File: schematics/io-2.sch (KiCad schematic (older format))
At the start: 8 parts, among them J13 FDC Connector, J13 Left Audio, J14 Right Audio, J9 IDE Connector, U11 WD1772, U12 EN5503DOC

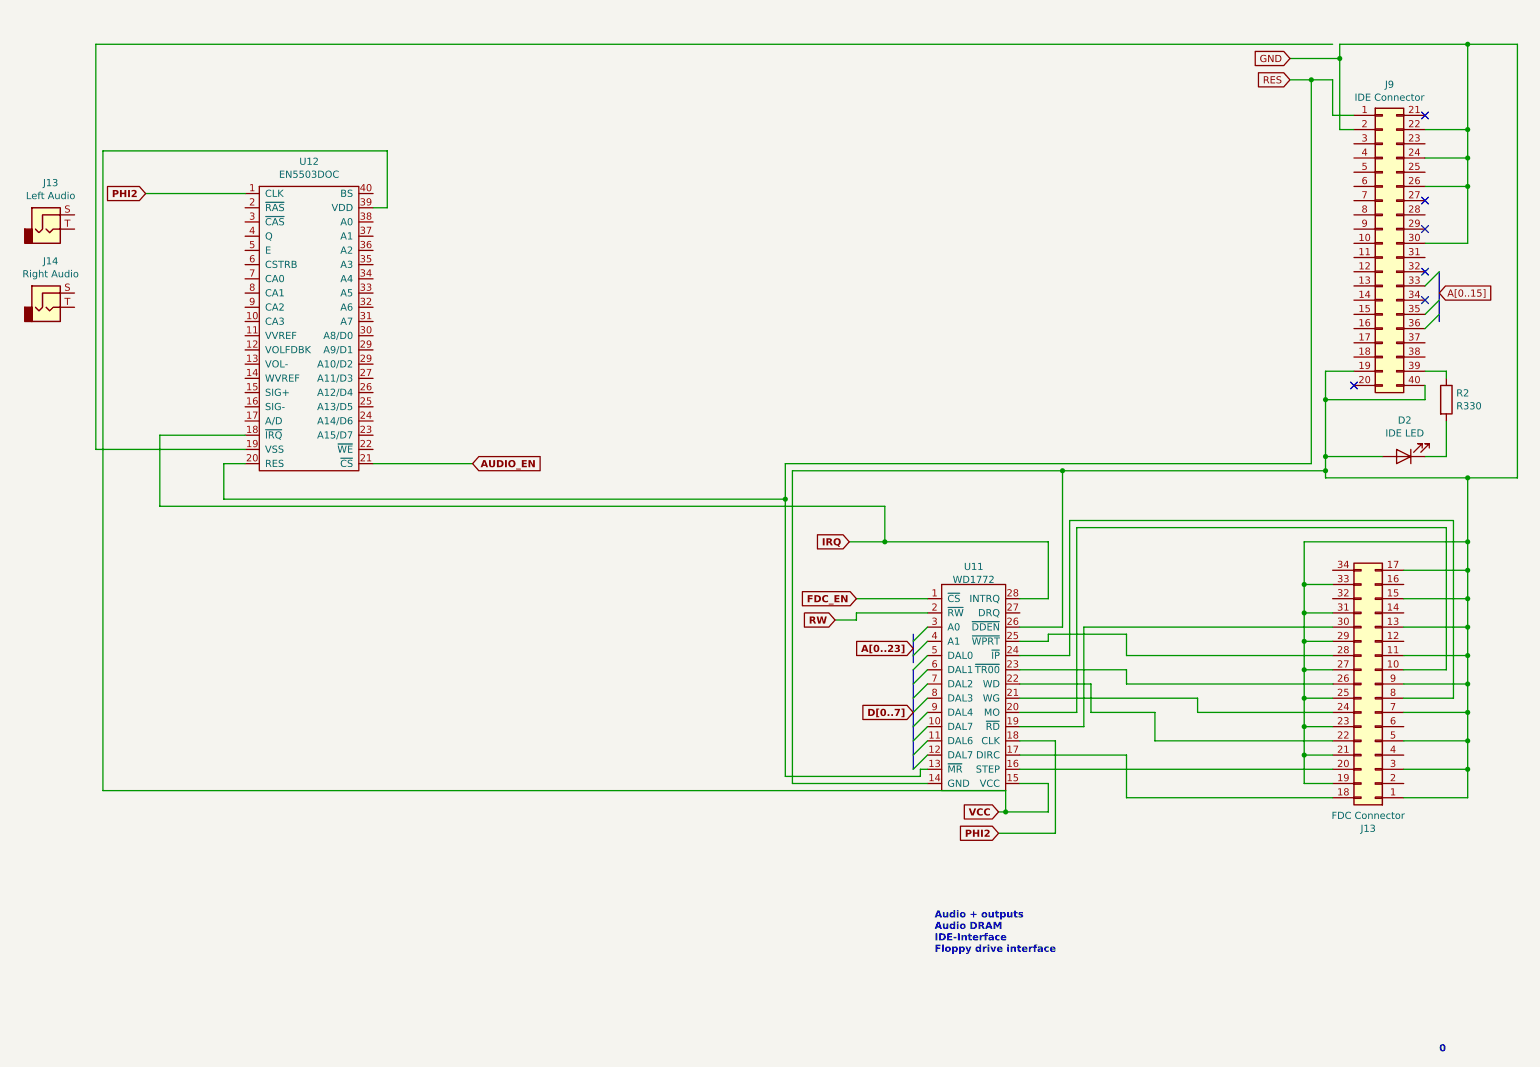
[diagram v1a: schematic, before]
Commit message: Removed EN5503DOC chip from IO2 sheet as it is now on it's own separate sheet. Changed description texts to reflect the change.
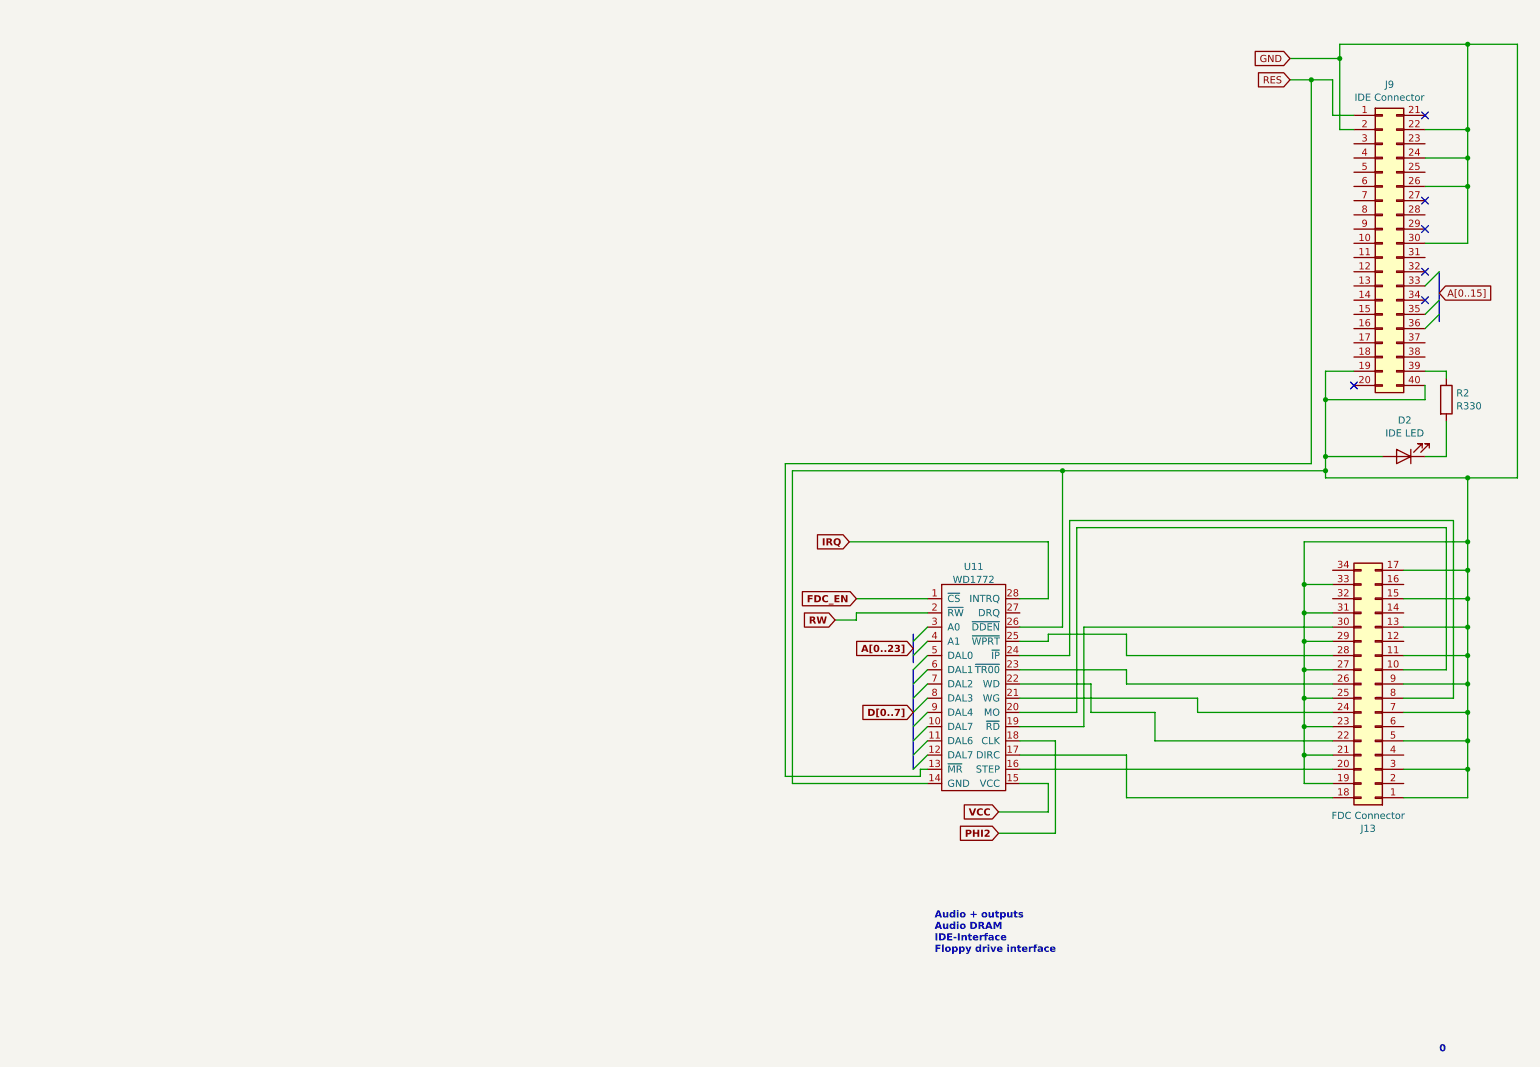
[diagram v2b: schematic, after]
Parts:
- removed J13: Left Audio, symbol Connector:AudioJack2
- removed J14: Right Audio, symbol Connector:AudioJack2
- removed U12: EN5503DOC, symbol prometh_custom:EN5503DOC
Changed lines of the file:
@@
 Wire Wire Line
 	7850 5750 7850 5950
-Wire Wire Line
-	7850 5950 7550 5950
 Text GLabel 6450 4050 0    50   Input ~ 10
 IRQ
@@
 	7850 4450 7850 4050
 Wire Wire Line
-	7850 4050 6700 4050
-Wire Wire Line
 	7650 4450 7850 4450
 Wire Wire Line
 	9700 3500 6000 3500
-Wire Wire Line
-	6000 3500 6000 3750
 Wire Wire Line
 	6000 5700 6950 5700
@@
 Wire Wire Line
 	7950 3550 6050 3550
-$Comp
-L prometh_custom:EN5503DOC U12
-U 1 1 5F1893D3
-P 2650 1500
-AR Path="/5F1893D3" Ref="U12"  Part="1"
-AR Path="/5F47C633/5F1893D3" Ref="U12"  Part="1"
-F 0 "U12" H 2650 1625 50  0000 C CNN
-F 1 "EN5503DOC" H 2650 1534 50  0000 C CNN
-F 2 "" H 2650 1500 50  0001 C CNN
-F 3 "" H 2650 1500 50  0001 C CNN
-	1    2650 1500
-	1    0    0    -1
-$EndComp
-Wire Wire Line
-	6700 4050 6700 3800
-Wire Wire Line
-	6700 3800 1600 3800
-Wire Wire Line
-	1600 3800 1600 3300
-Wire Wire Line
-	1600 3300 2200 3300
-Connection ~ 6700 4050
-Wire Wire Line
-	6700 4050 6450 4050
-Wire Wire Line
-	2050 3750 2050 3500
-Wire Wire Line
-	2050 3500 2200 3500
-Wire Wire Line
-	9850 550  1150 550
-Wire Wire Line
-	1150 550  1150 3400
-Wire Wire Line
-	1150 3400 2200 3400
 Wire Wire Line
 	6050 3550 6050 5750
-Wire Wire Line
-	2050 3750 6000 3750
-Connection ~ 6000 3750
-Wire Wire Line
-	6000 3750 6000 5700
-Wire Wire Line
-	7550 5950 7550 5800
-Wire Wire Line
-	7550 5800 1200 5800
-Wire Wire Line
-	1200 5800 1200 1300
-Wire Wire Line
-	1200 1300 3200 1300
-Wire Wire Line
-	3200 1300 3200 1700
-Wire Wire Line
-	3200 1700 3100 1700
-Connection ~ 7550 5950
-Wire Wire Line
-	7550 5950 7500 5950
-Text GLabel 3800 3500 2    50   Input ~ 10
-AUDIO_EN
-Wire Wire Line
-	3100 3500 3800 3500
-Text GLabel 1500 1600 0    50   Input ~ 10
-PHI2
-Wire Wire Line
-	1500 1600 2200 1600
-$Comp
-L Connector:AudioJack2 J13
-U 1 1 5F1E7CA0
-P 800 1850
-F 0 "J13" H 832 2175 50  0000 C CNN
-F 1 "Left Audio" H 832 2084 50  0000 C CNN
-F 2 "" H 800 1850 50  0001 C CNN
-F 3 "~" H 800 1850 50  0001 C CNN
-	1    800  1850
-	1    0    0    -1
-$EndComp
-$Comp
-L Connector:AudioJack2 J14
-U 1 1 5F1EC018
-P 800 2400
-F 0 "J14" H 832 2725 50  0000 C CNN
-F 1 "Right Audio" H 832 2634 50  0000 C CNN
-F 2 "" H 800 2400 50  0001 C CNN
-F 3 "~" H 800 2400 50  0001 C CNN
-	1    800  2400
-	1    0    0    -1
-$EndComp
 Wire Bus Line
 	10600 2150 10600 2500
@@
 Wire Bus Line
 	6900 4950 6900 5650
+Wire Wire Line
+	6000 3500 6000 5700
+Wire Wire Line
+	6450 4050 7850 4050
+Wire Wire Line
+	7500 5950 7850 5950
 $EndSCHEMATC

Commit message: Minor adjustment to io-2 sheet.
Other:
- note added: "IDE-Interface\nFloppy drive interface"
- note removed: "Audio + outputs\nAudio DRAM\nIDE-Interface\nFloppy drive interface"
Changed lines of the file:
@@
 Text Notes 10600 7650 0    50   ~ 10
 0
-Text Notes 7050 6950 0    50   ~ 10
-Audio + outputs\nAudio DRAM\nIDE-Interface\nFloppy drive interface
+Text Notes 7050 6750 0    50   ~ 10
+IDE-Interface\nFloppy drive interface
 $Comp
 L Connector_Generic:Conn_02x20_Top_Bottom J9

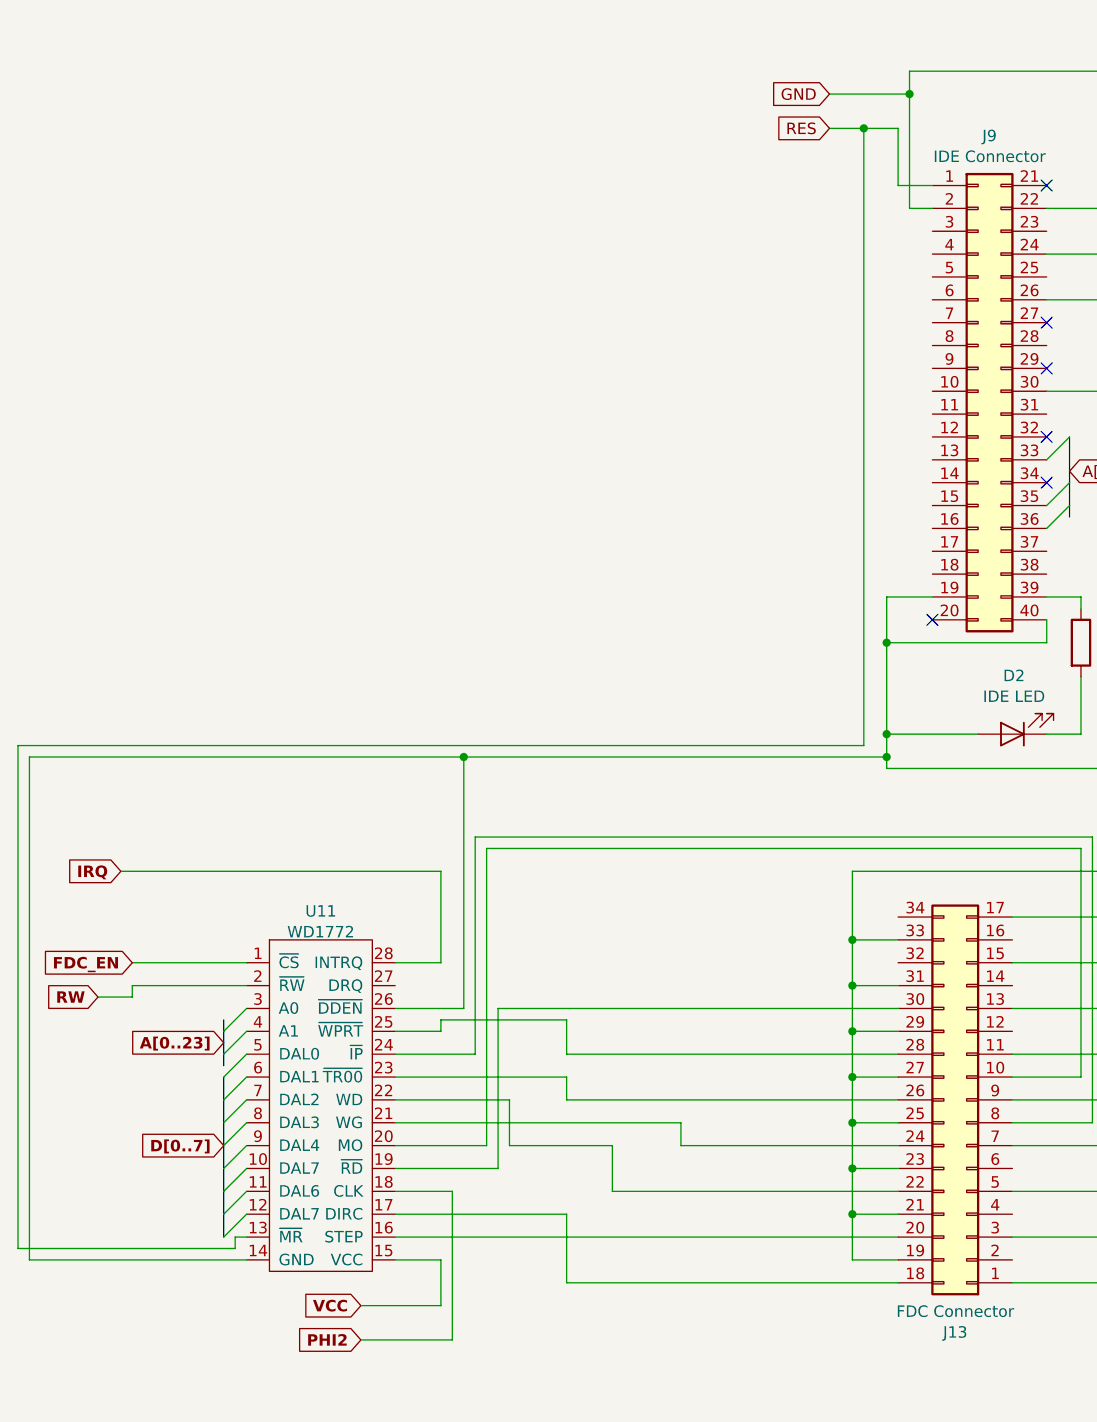
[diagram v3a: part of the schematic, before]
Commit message: Re-added 8->16bit IDE data handling via latches and buffers.
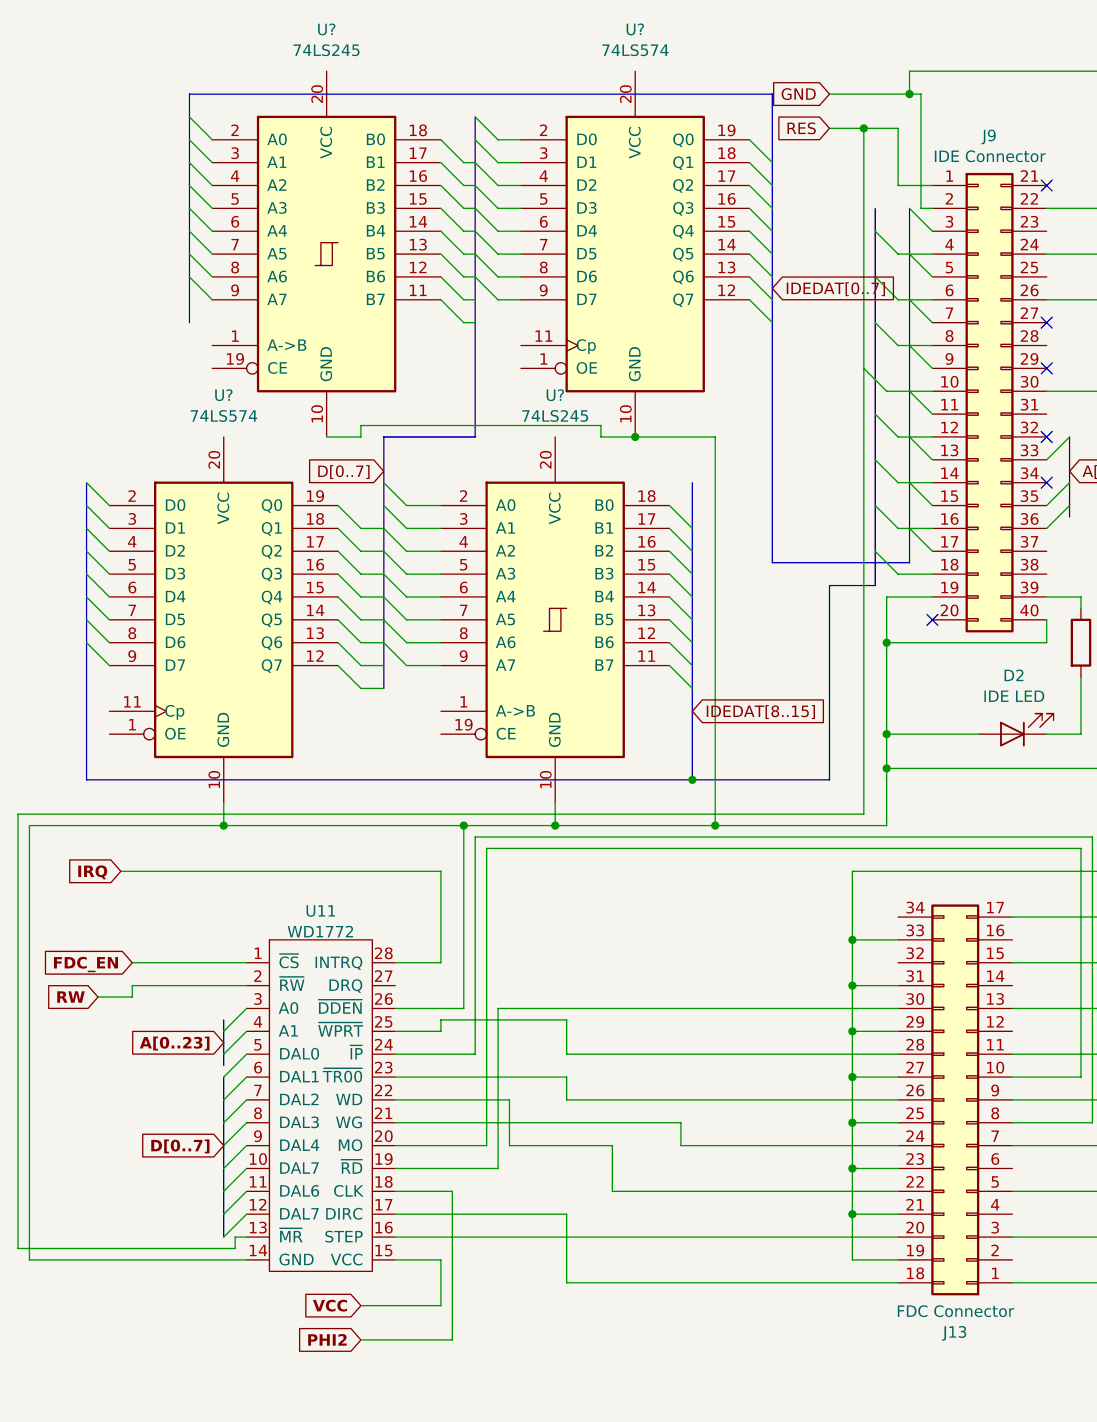
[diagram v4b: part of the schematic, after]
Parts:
- added U? (x2): 74LS574, symbol 74xx:74LS574
- added U? (x2): 74LS245, symbol 74xx:74LS245
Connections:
- net GND: now also U?.10 (GND), U?.10 (GND), U?.10 (GND), U?.10 (GND)
